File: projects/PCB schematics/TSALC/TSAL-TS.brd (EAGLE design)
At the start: 99.1 x 99.1 mm, 29 parts, among them J1 2P_1-770166-0, J2 2P_1-770166-0, J3 2P_1-770166-0, J4 2P_1-770166-0, X1 5566-2, X2 5566-2

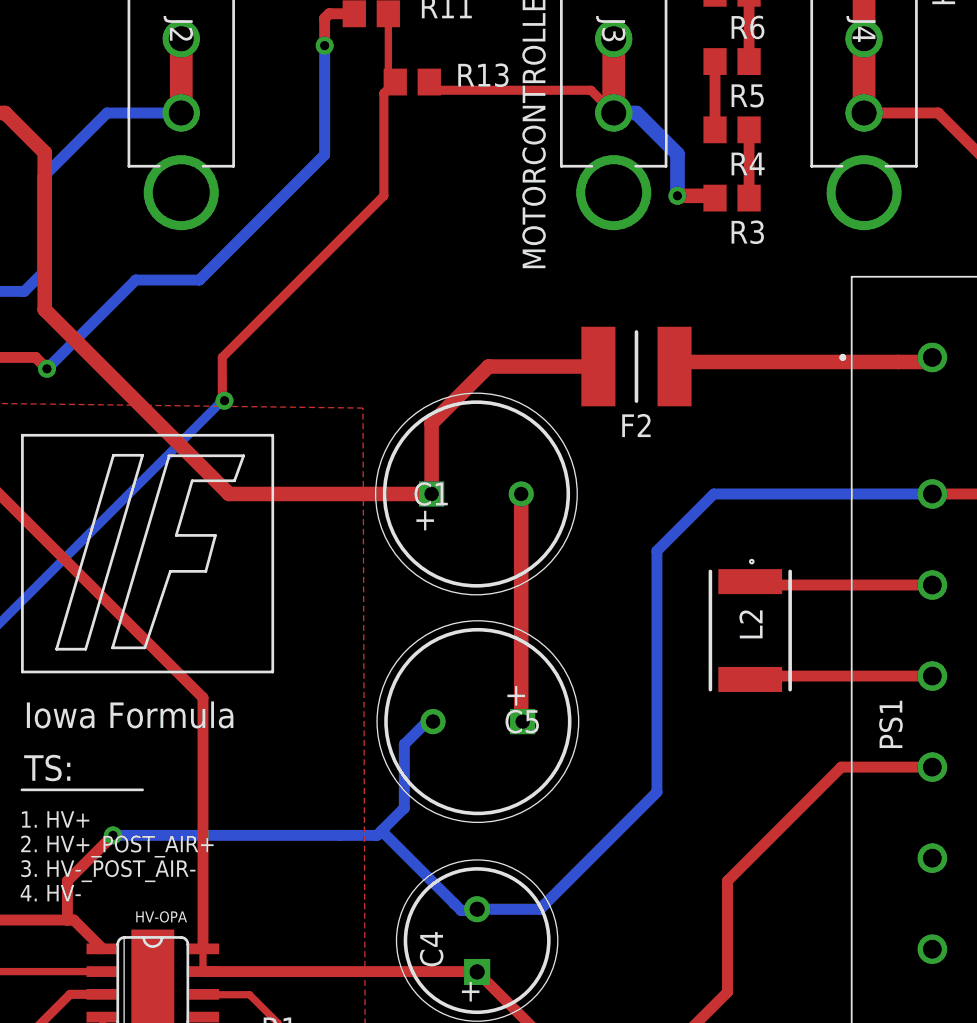
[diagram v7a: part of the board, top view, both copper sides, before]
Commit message: RTDS + TSAL Board update
Minor board & schematic errors corrected
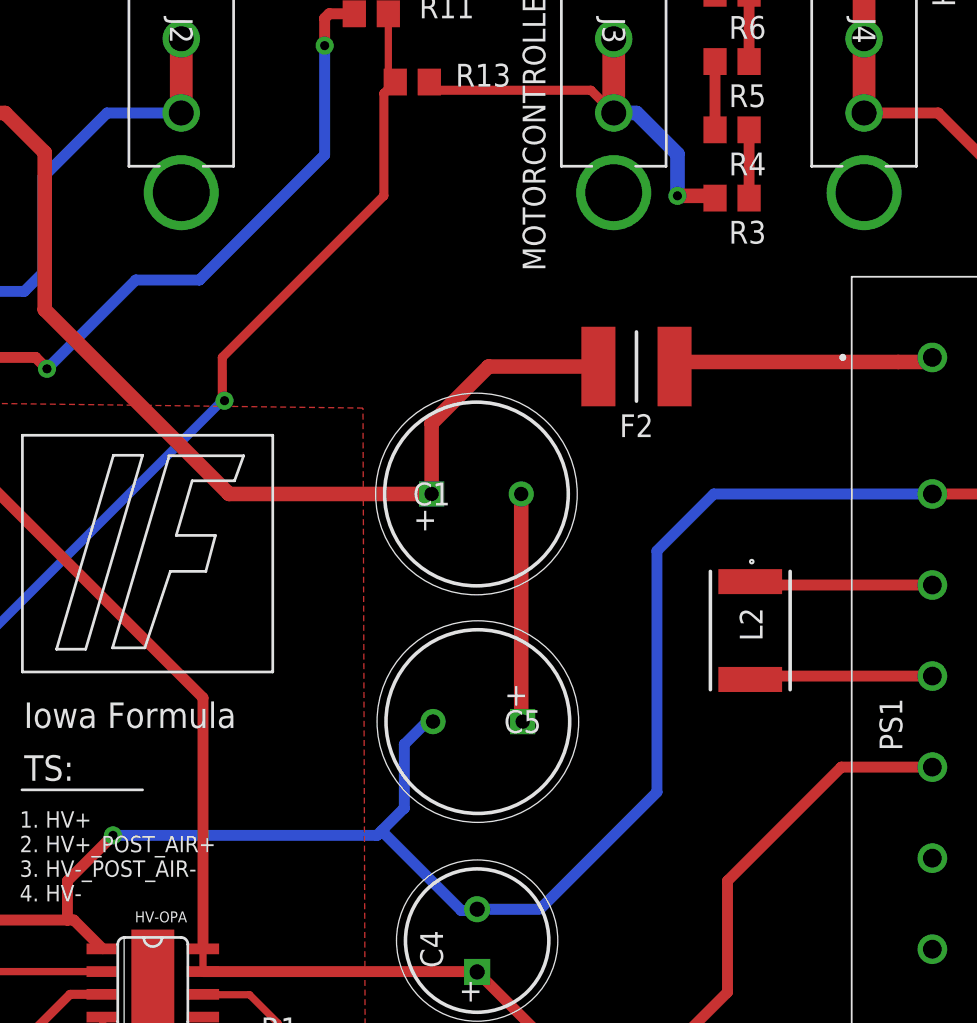
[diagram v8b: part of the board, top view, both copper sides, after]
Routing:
- net HV-: track 210.4 -> 209.6 mm
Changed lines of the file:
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@@
 <wire x1="87.63" y1="64.77" x2="80.01" y2="64.77" width="0.6096" layer="1"/>
 <wire x1="64.643" y1="48.133" x2="64.643" y2="61.595" width="0.6096" layer="16"/>
-<wire x1="64.643" y1="48.133" x2="58.42" y2="41.91" width="0.6096" layer="16"/>
-<wire x1="58.42" y1="41.91" x2="58.166" y2="41.656" width="0.6096" layer="16"/>
+<wire x1="58.166" y1="41.656" x2="64.643" y2="48.133" width="0.6096" layer="16"/>
 <wire x1="18.0315" y1="33.782" x2="18.0315" y2="37.4015" width="0.6096" layer="1"/>
 <wire x1="18.0315" y1="37.4015" x2="18.095" y2="37.465" width="0.6096" layer="1"/>
@@
 <wire x1="23.21625" y1="40.99625" x2="21.59" y2="39.37" width="0.6096" layer="1"/>
 <wire x1="91.44" y1="74.93" x2="91.44" y2="68.58" width="0.6096" layer="1"/>
-<wire x1="75.7682" y1="86.0298" x2="76.2" y2="86.0298" width="0.6096" layer="1"/>
 <wire x1="31.75" y1="40.99625" x2="31.75" y2="43.18" width="0.6096" layer="1"/>
 <wire x1="31.75" y1="43.18" x2="34.29" y2="45.72" width="0.6096" layer="1"/>
 <via x="34.29" y="45.72" extent="1-16" drill="0.508"/>
-<wire x1="34.29" y1="45.72" x2="46.99" y2="45.72" width="0.6096" layer="16"/>
-<wire x1="46.99" y1="45.72" x2="49.022" y2="45.72" width="0.6096" layer="16"/>
+<wire x1="34.29" y1="45.72" x2="49.022" y2="45.72" width="0.6096" layer="16"/>
 <wire x1="49.022" y1="45.72" x2="49.276" y2="45.974" width="0.6096" layer="16"/>
 <wire x1="49.276" y1="45.974" x2="50.546" y2="47.244" width="0.6096" layer="16"/>
@@
 <wire x1="17.145" y1="47.05" x2="17.145" y2="41.85" width="0.4064" layer="1"/>
 <contactref element="C5" pad="2"/>
-<wire x1="49.276" y1="45.974" x2="53.34" y2="41.91" width="0.6096" layer="16"/>
-<wire x1="53.721" y1="41.529" x2="53.34" y2="41.91" width="0.6096" layer="16"/>
+<wire x1="49.276" y1="45.974" x2="53.721" y2="41.529" width="0.6096" layer="16"/>
 <wire x1="76.2" y1="90.17" x2="76.2" y2="95.377" width="1.27" layer="1"/>
 <wire x1="76.2" y1="95.377" x2="75.057" y2="96.52" width="1.27" layer="1"/>
@@
 <wire x1="64.643" y1="61.595" x2="67.818" y2="64.77" width="0.6096" layer="16"/>
 <wire x1="67.818" y1="64.77" x2="80.01" y2="64.77" width="0.6096" layer="16"/>
-<wire x1="58.42" y1="41.91" x2="58.11" y2="41.6" width="0.6096" layer="16"/>
-<wire x1="58.11" y1="41.6" x2="54.61" y2="41.6" width="0.6096" layer="16"/>
+<wire x1="54.61" y1="41.6" x2="58.11" y2="41.6" width="0.6096" layer="16"/>
 <wire x1="54.61" y1="41.6" x2="54.539" y2="41.529" width="0.6096" layer="16"/>
 <wire x1="54.539" y1="41.529" x2="53.721" y2="41.529" width="0.6096" layer="16"/>
 <wire x1="50.546" y1="50.8" x2="51.816" y2="52.07" width="0.6096" layer="16"/>
 <wire x1="51.816" y1="52.07" x2="52.15" y2="52.07" width="0.6096" layer="16"/>
+<wire x1="58.11" y1="41.6" x2="58.166" y2="41.656" width="0.2032" layer="16"/>
 </signal>
 <signal name="VCC">
